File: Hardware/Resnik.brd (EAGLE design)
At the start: 64.8 x 100 mm, 195 parts, among them IC1 ATMEGA644M, J1 CONN_82.54_SCREW, J3 CONN_42.54_SCREW, J4 CONN_82.54_SCREW, Q1 DMG3404, Q2 DMG3404, Q3 FDN360P, Q4 FDN360P, Q5 FDN360P, Q6 DMG3404, U1 TLV61220DBV, U10 TPS22917DBV, U11 SN74AUP1G04YFP, U12 SN74AUP1G04YFP, U13 SN74AUP2G86SOT833-1, U14 SN74AUP2G08DQE, U15 SN74AUP2G08DQE, U16 SN74AUP2G08DQE, U17 MIC2544MSOP, U18 MIC2544MSOP, U19 MIC2544MSOP, U2 TPS62822DLC, U20 MIC2544MSOP, U21 TPS22917DBV, U22 TPS22917DBV, U23 FT231X-Q, U24 SN74LVC1G3157DRL, U25 SN74AUP3G34DCU, U26 TXS0102DQM, U27 TXS0108RGY, U28 TXS0108RGY, U29 TXS0104RGY, U3 TPS61032RSA, U30 MCP4726A2SOT-23, U31 BME280, U32 ADS1115, U33 ADS1115, U34 INA211DCK, U35 INA210DCK, U36 TCA9535RTW, U37 TLV3691DCK, U38 TS5A21366RSE, U39 MIC94090C6, U5 BQ2980RUG, U6 TPS2105, U7 LTC4412S6, U8 TPL5111DDC, U9 TPS79733

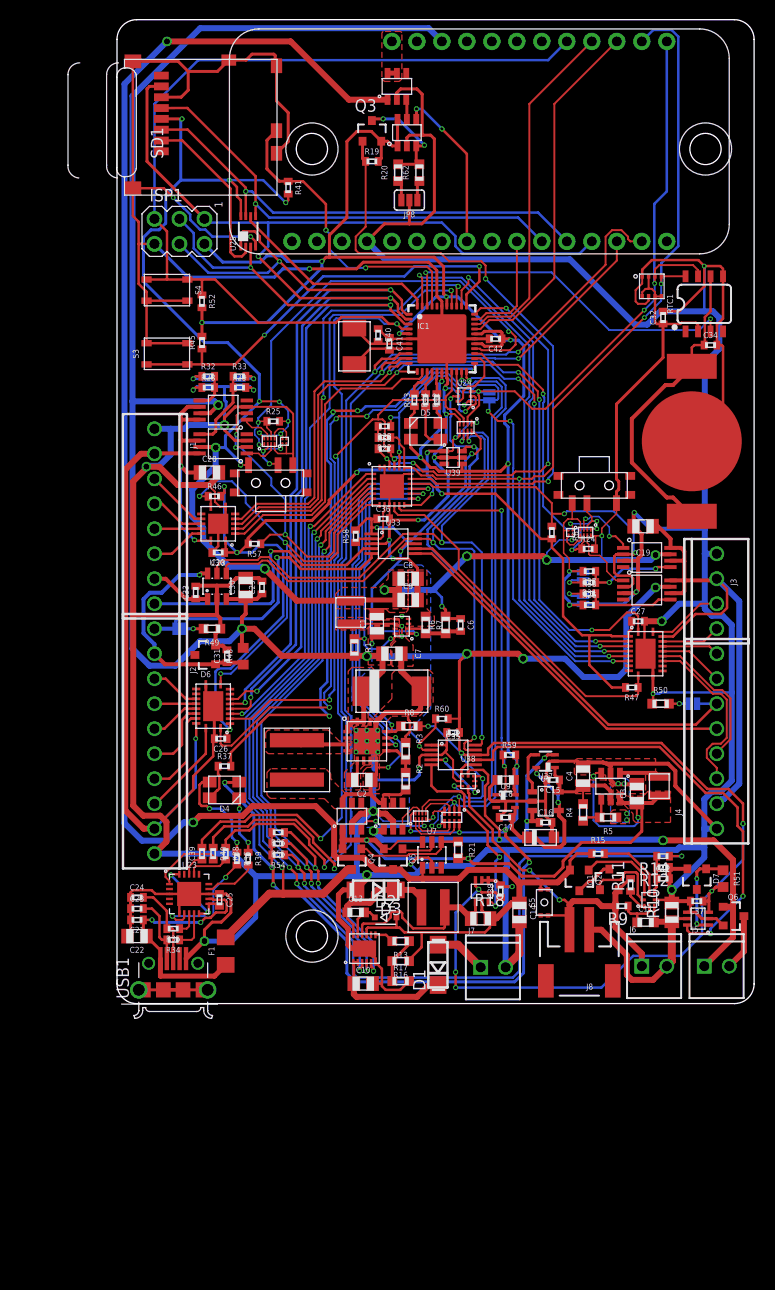
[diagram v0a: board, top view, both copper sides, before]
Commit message: Initial updates for v0.3
Additional routing required, need to add ADC switch enable, need to add efficiency modification to mppt
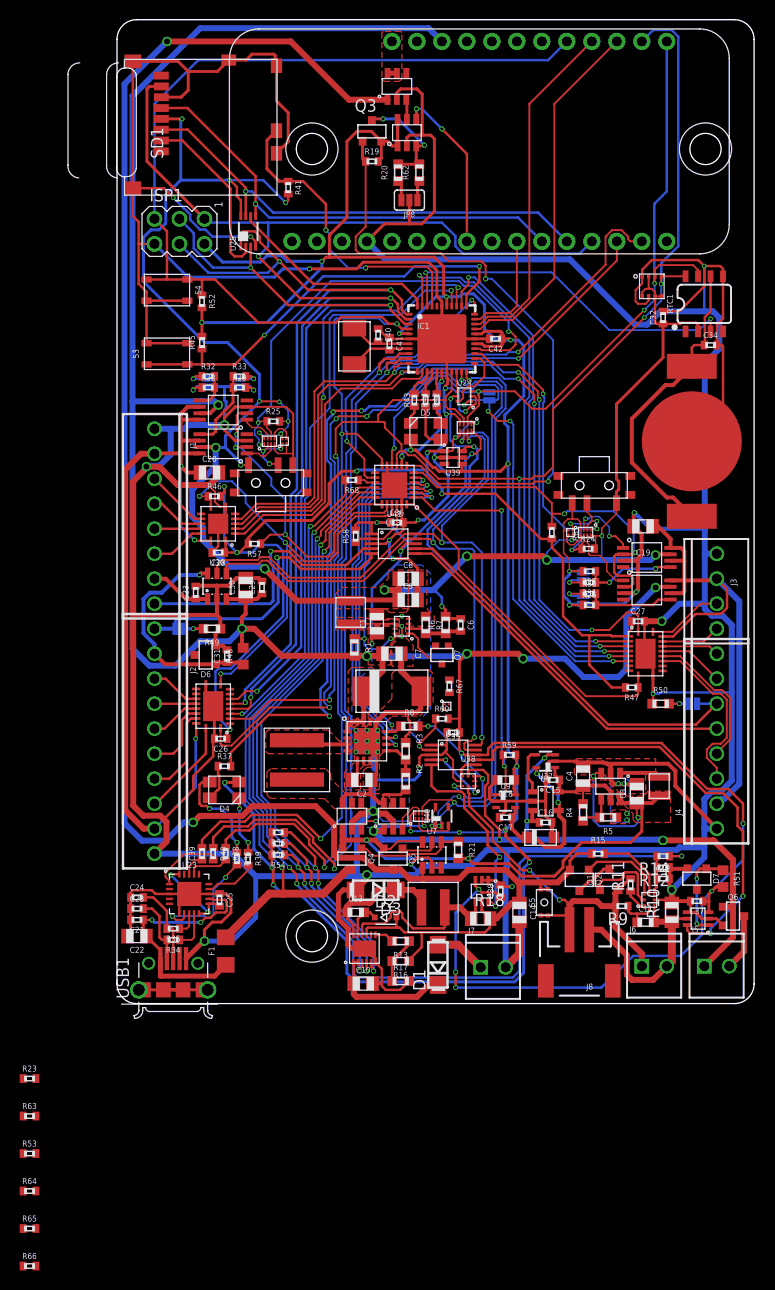
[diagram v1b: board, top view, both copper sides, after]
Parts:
- removed R22: (no value), bschulz_passives:R0402
- removed U36: TCA9535RTW, bschulz:RTW_S-PWQFN-N24
- added Q7: 2N7002, bschulz:SOT323
- added R63: 100k, bschulz_passives:R0402
- added R64, R68: 1M, bschulz_passives:R0402
- added R65, R66: 180k, bschulz_passives:R0402
- added R67: 10k, bschulz_passives:R0402
- added U40: SN74AHC1G86DCK, bschulz:DCK_R-PDSO-G5
- added U41: MCP23018QFN, bschulz:QFN24
- R23: value (none) -> 100k
- R53: value 10k -> 1M
- U13: value SN74AUP2G86SOT833-1 -> SN74AUP1G04YFP; device bschulz:SOT833-1 -> bschulz:DSBGD_4
- moved R53 80.2 mm to (-8.89, -15.2)
- moved R23 75.5 mm to (-8.89, -7.62), turned to 0 degrees
- moved U13 11.3 mm to (33.5, 30.2), turned to 0 degrees
- moved C36 1.45 mm to (28.4, 48.9)
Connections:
- removed net N$22: U13.7, U16.1
- removed net N$25: U13.3, U16.5
- new net N$17: R68.1, U41.15
- new net N$68: Q7.1, U13.B2
- new net POWER_EN: U13.A1, U16.1, U16.5, U2.1, U3.11, U40.4
- new net VCC: U40.5
- net 3V3_AUX_PG: now also U41.2; no longer U36.13
- net 3V3_CORE: now also U13.A2, U41.8; no longer R22.2, R23.2, R53.2, U13.8, U36.21
- net 3V3_CORE_ISO: now also R23.2
- net 5V_AUX: now also Q7.3, R67.2; no longer U2.1
- net ADC_EXT_ALERT: now also U41.22; no longer U36.8
- net ADC_OB_ALERT: now also U41.4; no longer U36.15
- net BMS_CTR: now also U41.16; no longer U36.2
- net BUS_LOGIC_EN_PRIME: now also U41.21; no longer U36.7
- net BUS_LOGIC_EN_SEC: now also U41.24; no longer U36.10
- net C0: now also U40.1, U40.2; no longer U13.1, U13.6
- net C1: no longer U13.2, U13.5
- net FAULT_PRIME: now also U41.20; no longer U36.6
- net FAULT_SEC: now also U41.6; no longer U36.16
- net FEATHER_EN: now also U41.7; no longer U36.17
- net GLOBAL_INT: now also U41.14; no longer R53.1, U36.22
- net GND: now also Q7.2, R23.1, R53.1, R63.1, R64.1, R65.1, R66.1, R67.1, U13.B1, U40.3, U41.11, U41.23, U41.EP; no longer U13.4, U36.18, U36.23, U36.24, U36.9, U36.EP
- net LBI: now also U41.3; no longer U36.14
- net MPPT_CHRG: now also U41.18; no longer U36.4
- net MPPT_FAULT: now also U41.19; no longer U36.5
- net MPPT_SHDN: now also U41.17; no longer U36.3
- net PG_LDO: now also U41.1; no longer U36.11
- net RST: now also U41.12
- net SCL: now also U41.9; no longer R22.1, U36.19
- net SDA_OB: now also U41.10; no longer R23.1, U36.20
- net VBUS_PRIME: now also R65.2
- net VBUS_SEC: now also R66.2
- net VUSB_POWER: now also R63.2, R68.2; no longer U36.1
- net V_HP: no longer U3.11
- net V_HP_SYNC: now also U41.5; no longer U36.12
- net V_LI_SENSE: now also R64.2
- net V_PRIME_SENSE: now also R53.2
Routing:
- net GLOBAL_INT: track 41.1 -> 28.3 mm, vias 4 -> 2
- net V_HP: track 20.5 -> 14.6 mm, vias 2 -> 0
- net N$22: track 5.89 -> 0.00 mm
- net RST: track 169.5 -> 175.3 mm, vias 2 -> 3
- net 3V3_CORE: track 261.2 -> 256.5 mm
- net 5V_AUX: track 355.5 -> 350.8 mm, vias 20 -> 19
- net POWER_EN: track 0.00 -> 4.51 mm, vias 0 -> 1
- net GND: track 857.9 -> 853.7 mm
- net V_HP_SYNC: track 40.5 -> 36.5 mm
- net N$25: track 3.67 -> 0.00 mm
- net 3V3_AUX_PG: track 25.7 -> 28.5 mm
- net VUSB_POWER: track 65.9 -> 63.7 mm
- net BUS_LOGIC_EN_PRIME: track 46.2 -> 48.0 mm
- net N$17: track 0.00 -> 1.82 mm
- net SCL: track 162.3 -> 164.1 mm
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
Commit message: Layout updates, cleanup required, minor testing
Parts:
- removed R54: (no value), bschulz_passives:R0402
- added Q8: 2N7002, bschulz:SOT323
- added R22, R69, R70, R71: (no value), bschulz_passives:R0603
- moved R66 103.6 mm to (62.9, 48.0)
- moved R65 84.8 mm to (4.57, 60.8)
- moved R23 72.3 mm to (52.2, 31.0), turned to 180 degrees
- moved R63 27.0 mm to (10.4, 7.49), turned to 270 degrees
- moved U13 3.22 mm to (34.0, 33.4), turned to 90 degrees
- moved F1 1.15 mm to (12.2, 5.46)
- moved R67 0.74 mm to (34.2, 31.6), turned to 0 degrees
- moved U38 0.25 mm to (35.4, 22.6)
- moved Q7 0.18 mm to (33.1, 35.6), turned to 270 degrees
- moved R47 0.13 mm to (52.2, 32.1)
- moved U40 0.13 mm to (33.1, 19.1)
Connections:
- removed net N$67: C10.1, D1.C, U4.1, U4.2
- removed net VCC: U40.5
- new net ADC_SENSE_SW: IC1.40, U38.3, U38.7
- new net MPPT_VIN_REG: R22.1, R69.2, U4.2
- new net N$22: Q8.3, R70.1
- new net V_SOLAR_IN: C10.1, D1.C, R22.2, R71.2, U4.1
- net 3V3_CORE: now also U40.5; no longer R54.2
- net 5V_AUX: no longer U38.3, U38.7
- net C0: no longer U40.2
- net C1: now also U40.2
- net GND: now also Q8.2, R69.1
- net MPPT_CHRG: now also Q8.1
- net MPPT_SHDN: now also R70.2, R71.1; no longer R54.1, U41.17
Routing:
- net ADC_SENSE_SW: track 0.00 -> 68.0 mm, vias 0 -> 5
- net MPPT_SHDN: track 62.5 -> 13.3 mm, vias 4 -> 2
- net POWER_EN: track 4.51 -> 39.4 mm, vias 1 -> 3
- net GND: track 853.7 -> 881.1 mm, vias 36 -> 38
- net V_SOLAR_IN: track 0.00 -> 22.2 mm
- net N$67: track 12.9 -> 0.00 mm
- net 3V3_CORE: track 256.5 -> 269.2 mm, vias 17 -> 22
- net MPPT_VIN_REG: track 0.00 -> 8.51 mm, vias 0 -> 2
- net VBUS_SEC: track 52.7 -> 60.3 mm
- net N$22: track 0.00 -> 6.74 mm
- net 5V_AUX: track 350.8 -> 346.5 mm, vias 19 -> 18
- net N$68: track 0.00 -> 3.83 mm
- net MPPT_CHRG: track 63.3 -> 65.6 mm
- net VUSB_POWER: track 63.7 -> 65.9 mm
- net VBUS_PRIME: track 82.5 -> 84.2 mm
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
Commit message: Continued layout, generated gerbers
Improved layout, generated gerbers, final design review before send to fab
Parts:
- added D8: BAT54C, bschulz:SOT23-3
- R18: value 5m -> 50m
- moved R64 59.3 mm to (32.5, 23.4)
- moved R53 55.8 mm to (32.5, 22.2)
- moved U37 0.52 mm to (44.1, 24.8), turned to 180 degrees
- moved U32 0.25 mm to (34.2, 25.5)
- moved C35 0.25 mm to (34.2, 27.8)
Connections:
- new net N$69: D8.3, U37.5
- net 5V_LP: now also D8.2
- net V_CORE: no longer U37.5
- net V_PRIME: now also D8.1
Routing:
- net V_PRIME_SENSE: track 2.52 -> 12.5 mm, vias 0 -> 2
- net N$69: track 0.00 -> 6.88 mm, vias 0 -> 2
- net 5V_LP: track 11.2 -> 17.1 mm, vias 0 -> 2
- net GND: track 881.1 -> 886.7 mm
- net V_CORE: track 17.5 -> 12.1 mm, vias 2 -> 0
- net 3V3_CORE: track 269.2 -> 271.0 mm
- net V_LI_SENSE: track 6.64 -> 8.45 mm
- net V_CORE_SW: track 4.61 -> 3.19 mm
- net V_PRIME: track 74.9 -> 76.1 mm
- net I_LI: track 47.8 -> 48.5 mm
- net SCL: track 164.1 -> 163.4 mm
- net ADC_SENSE_SW: track 68.0 -> 67.4 mm
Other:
- board text added: "Project Resnik v0.3 ---------------- Developed by Northern Widget and University of Minnesota"
- board text removed: "Project Resnik v0.2 ---------------- Developed by Northern Widget and University of Minnesota"

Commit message: Naming/part cleanup
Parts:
- R12: value (none) -> 1k
- R22: value (none) -> 143k
- R51: value (none) -> 20k; device bschulz:R0603 -> bschulz_passives:R0603
- R55, R56, R59, R71: value (none) -> 1M
- R57, R58, R60, R61, R69: value (none) -> 100k
- R70: value (none) -> 200k

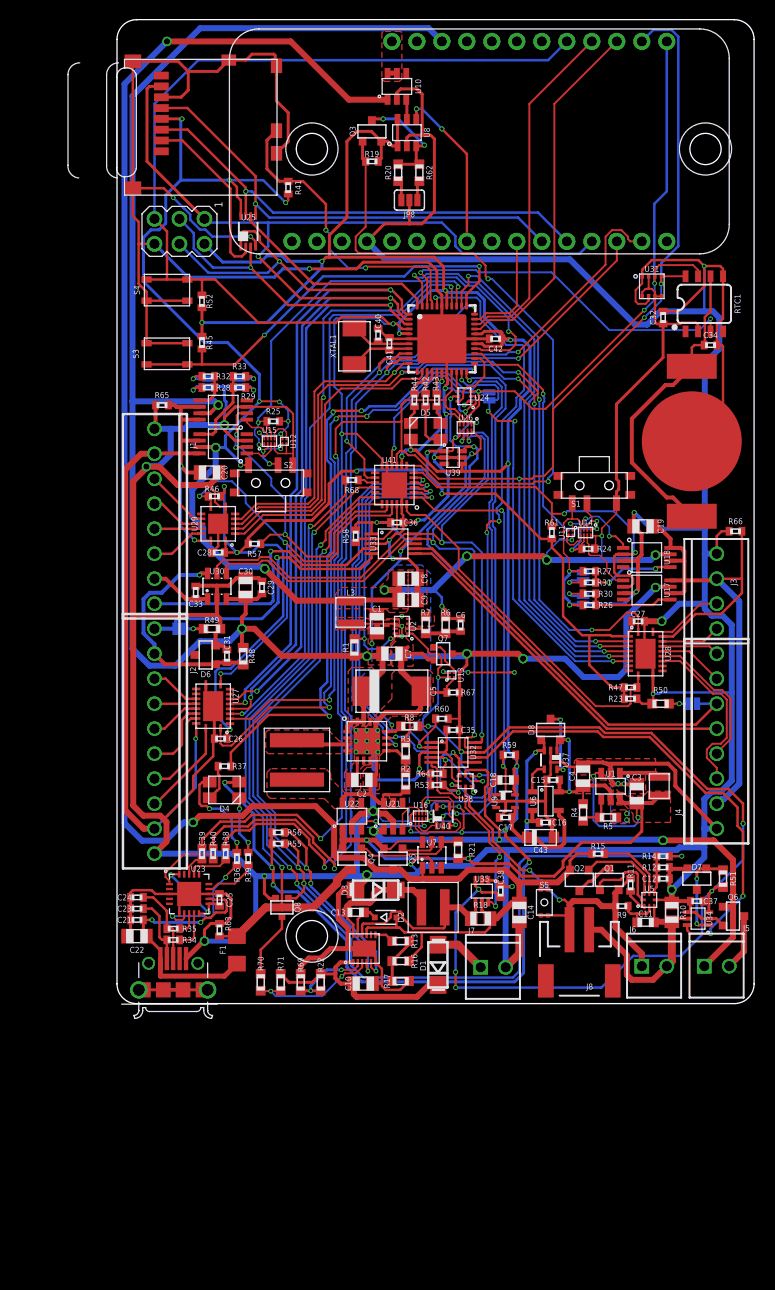
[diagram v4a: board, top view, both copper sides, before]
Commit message: Hardware fixes, review and verification required, gerber generated
Gerber generated and sent to DFM, verification and review required
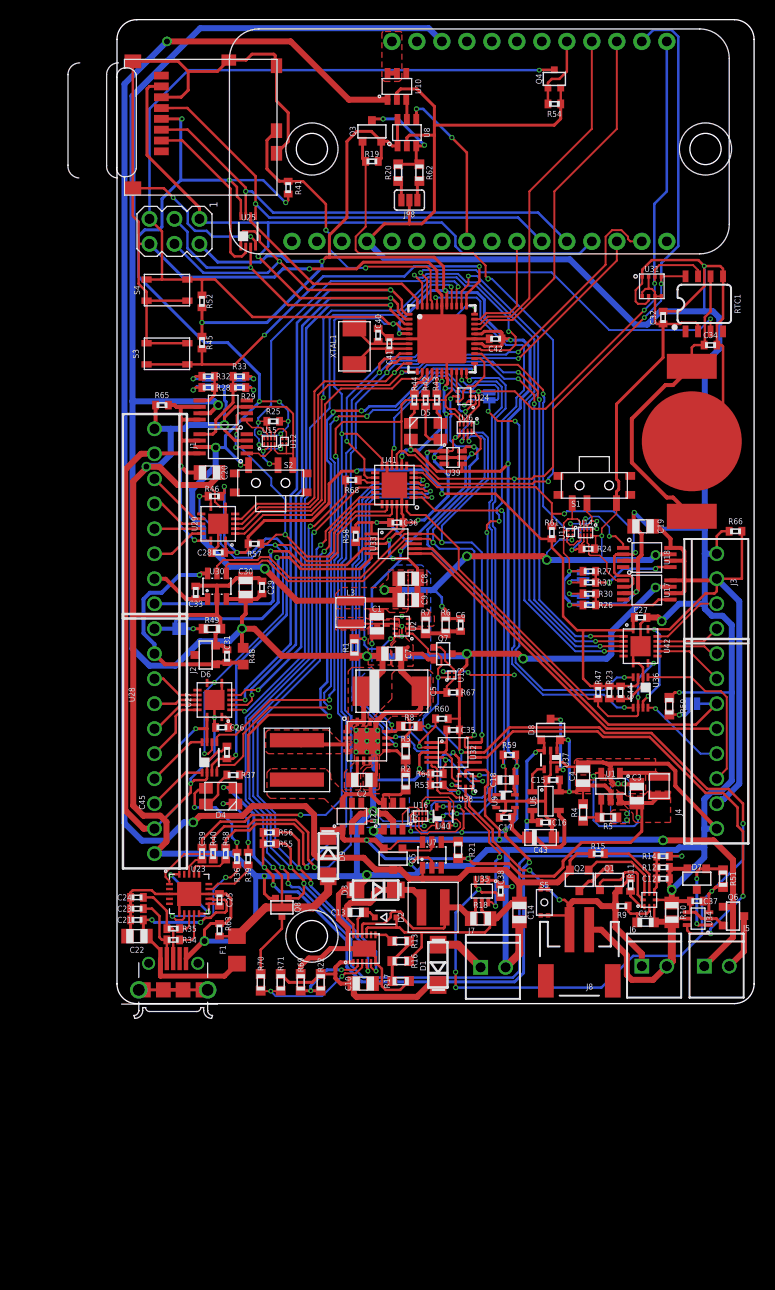
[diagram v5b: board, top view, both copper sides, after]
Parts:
- added C44, C45: 0.1uF, bschulz_passives:C0402
- added D9: (no value), bschulz:DO214AC
- added R54: (no value), bschulz_passives:R0402
- added U36: TCA9406DCU, bschulz:DCU_(R-PDSO-G8)
- added U42: TXS0104RGY, bschulz:RGY_S-PVQFN-N14
- Q4: value FDN360P -> 2N7002; device bschulz:SOT23-3 -> bschulz:SOT323
- U27: value TXS0108RGY -> TXS0104RGY; device bschulz:RGY_S-PVQFN-N20 -> bschulz:RGY_S-PVQFN-N14
- U28: value TXS0108RGY -> TCA9406DCU; device bschulz:RGY_S-PVQFN-N20 -> bschulz:DCU_(R-PDSO-G8)
- moved Q4 81.9 mm to (44.5, 94.0), turned to 0 degrees
- moved U28 45.6 mm to (9.40, 25.0), turned to 0 degrees
- moved R47 3.34 mm to (48.9, 31.6), turned to 90 degrees
- moved R23 2.25 mm to (50.0, 31.6), turned to 90 degrees
- moved R37 1.26 mm to (11.8, 23.2)
- moved C26 1.15 mm to (10.7, 28.1)
- moved R50 0.92 mm to (56.1, 30.2), turned to 270 degrees
- moved R55 0.89 mm to (15.5, 16.3)
- moved R56 0.89 mm to (15.5, 17.4)
- moved D4 0.74 mm to (10.5, 21.1)
- moved U27 0.65 mm to (9.91, 30.9)
- moved ISP1 0.51 mm to (5.84, 78.5)
- moved C27 0.46 mm to (53.2, 39.2)
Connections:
- new net RST_TRIG: MS1.21, Q4.1, R54.2
- net 3V3_CORE_ISO: now also C44.1, C45.1, U27.1, U28.3, U36.3, U42.1; no longer U27.2, U28.2
- net ADC_0: now also J1.8, U33.4; no longer J2.1, JP6.1, U33.5
- net ADC_1: now also J2.1, JP6.1, U33.5; no longer J1.8, U33.4
- net BUS_LOGIC_EN_PRIME: now also U27.8, U28.6; no longer U27.10
- net BUS_LOGIC_EN_SEC: now also U36.6, U42.8; no longer U28.10
- net CS_EXT: now also U27.2; no longer U27.4
- net CS_OUT: now also U27.13; no longer U27.17
- net GND: now also C44.2, C45.2, Q4.2, R54.1, U27.7, U28.2, U36.2, U42.7, U42.EP; no longer U27.11, U28.11, U28.EP
- net GPIO_2: now also U42.5; no longer U28.5
- net GPIO_2_OUT: now also U42.10; no longer U28.16
- net GPIO_3: now also U42.4; no longer U28.4
- net GPIO_3_OUT: now also U42.11; no longer U28.17
- net MISO: now also U27.3; no longer U27.5
- net MISO_OUT: now also U27.12; no longer U27.16
- net MOSI: now also U27.4; no longer U27.6
- net MOSI_OUT: now also U27.11; no longer U27.15
- net N$46: no longer Q4.1
- net RST: now also Q4.3; no longer MS1.21
- net RX_EXT: now also U42.2; no longer U28.1
- net RX_OUT_SEC: now also U42.13; no longer U28.20
- net SCK: now also U27.5; no longer U27.7
- net SCK_OUT: now also U27.10; no longer U27.14
- net SCL: now also U28.5, U36.5; no longer U27.3, U28.6
- net SCL_OUT_PRIME: now also U28.8; no longer U27.18
- net SCL_OUT_SEC: now also U36.8; no longer U28.15
- net SDA_EXT: now also U28.4, U36.4; no longer U27.1, U28.7
- net SDA_OUT_PRIME: now also U28.1; no longer U27.20
- net SDA_OUT_SEC: now also U36.1; no longer U28.14
- net TX_EXT: now also U42.3; no longer U28.3
- net TX_OUT_SEC: now also U42.12; no longer U28.18
- net VBUS_PRIME: now also U27.14, U28.7; no longer U27.19
- net VBUS_SEC: now also U36.7, U42.14; no longer U28.19
- net VUSB_POWER: now also D9.A; no longer Q4.3
- net V_BETA: now also D9.C; no longer Q4.2
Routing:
- net GND: track 886.7 -> 911.4 mm, vias 38 -> 40
- net BUS_LOGIC_EN_PRIME: track 48.0 -> 58.4 mm, vias 3 -> 4
- net SCL: track 163.4 -> 173.3 mm
- net N$46: track 11.1 -> 1.80 mm
- net 3V3_CORE_ISO: track 116.8 -> 126.0 mm, vias 8 -> 9
- net RST_TRIG: track 0.00 -> 7.59 mm
- net SDA_EXT: track 106.7 -> 114.2 mm
- net VBUS_SEC: track 60.3 -> 67.7 mm, vias 0 -> 2
- net SCL_OUT_SEC: track 14.9 -> 8.93 mm, vias 0 -> 1
- net RST: track 174.9 -> 169.1 mm, vias 3 -> 4
- net BUS_LOGIC_EN_SEC: track 36.5 -> 41.1 mm, vias 0 -> 2
- net SDA_OUT_PRIME: track 9.92 -> 6.14 mm
- net RX_EXT: track 81.9 -> 78.2 mm
- net 5V_AUX: track 346.8 -> 343.4 mm
- net VBUS_PRIME: track 84.2 -> 87.4 mm
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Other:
- board text added: "A2"
- board text added: "A3"
- board text added: "Project Resnik v0.4 ---------------- Developed by Northern Widget and University of Minnesota"
- board text removed: "Project Resnik v0.3 ---------------- Developed by Northern Widget and University of Minnesota"

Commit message: Silk screen edits, generated gerbers, v0.4 send to fab
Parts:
- moved U$4 1.78 mm to (16.9, 64.5)
- moved USB1 0.13 mm to (5.71, 1.52)
- moved C21 0.13 mm to (2.16, 8.51)
- moved C22 0.13 mm to (2.16, 6.86)
- moved C23 0.13 mm to (2.16, 9.65)
- moved C24 0.13 mm to (2.16, 10.8)
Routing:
- net GND: track 911.4 -> 910.3 mm
